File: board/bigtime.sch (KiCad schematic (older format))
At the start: 31 parts, among them IC1 NPIC6C596A, IC2 TPS62152, P1 CONN_IN, P2 CONN_OUT, U1 SA40-19, X1 MOUNTING_HOLE, X2 MOUNTING_HOLE, X3 MOUNTING_HOLE, X4 MOUNTING_HOLE

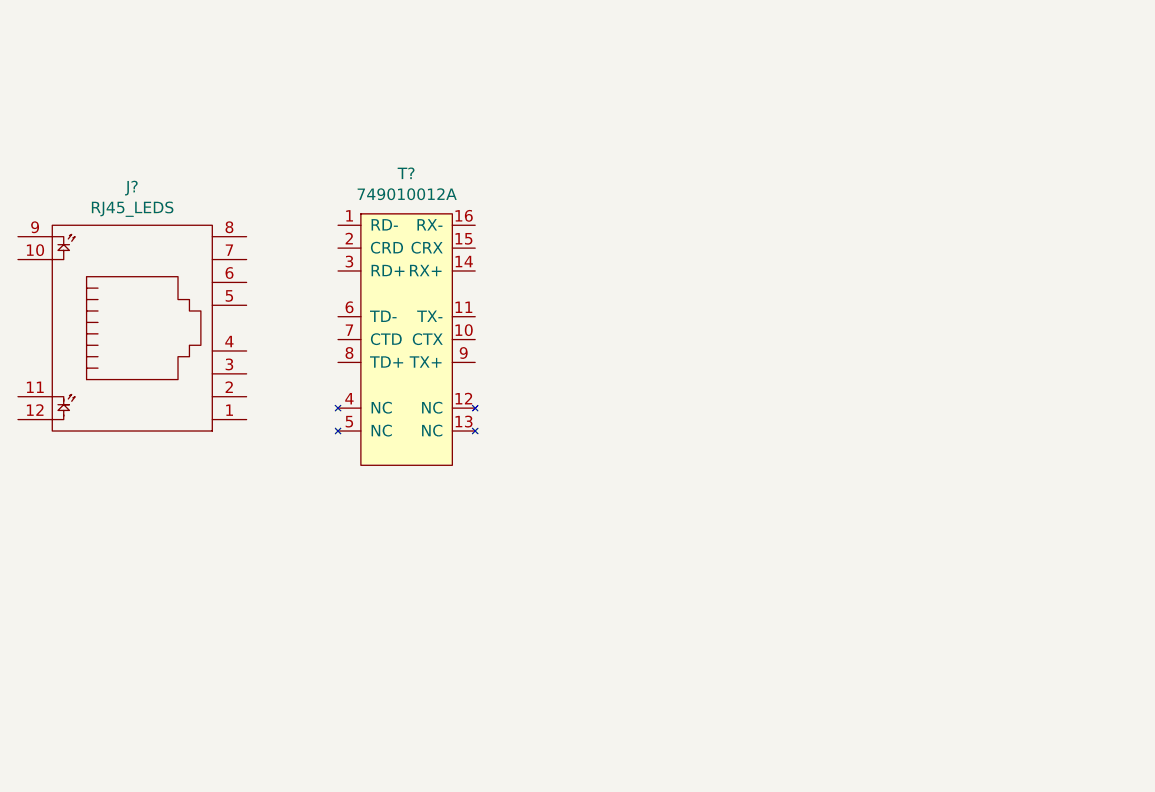
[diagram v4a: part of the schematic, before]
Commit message: separate sheet for ethernet
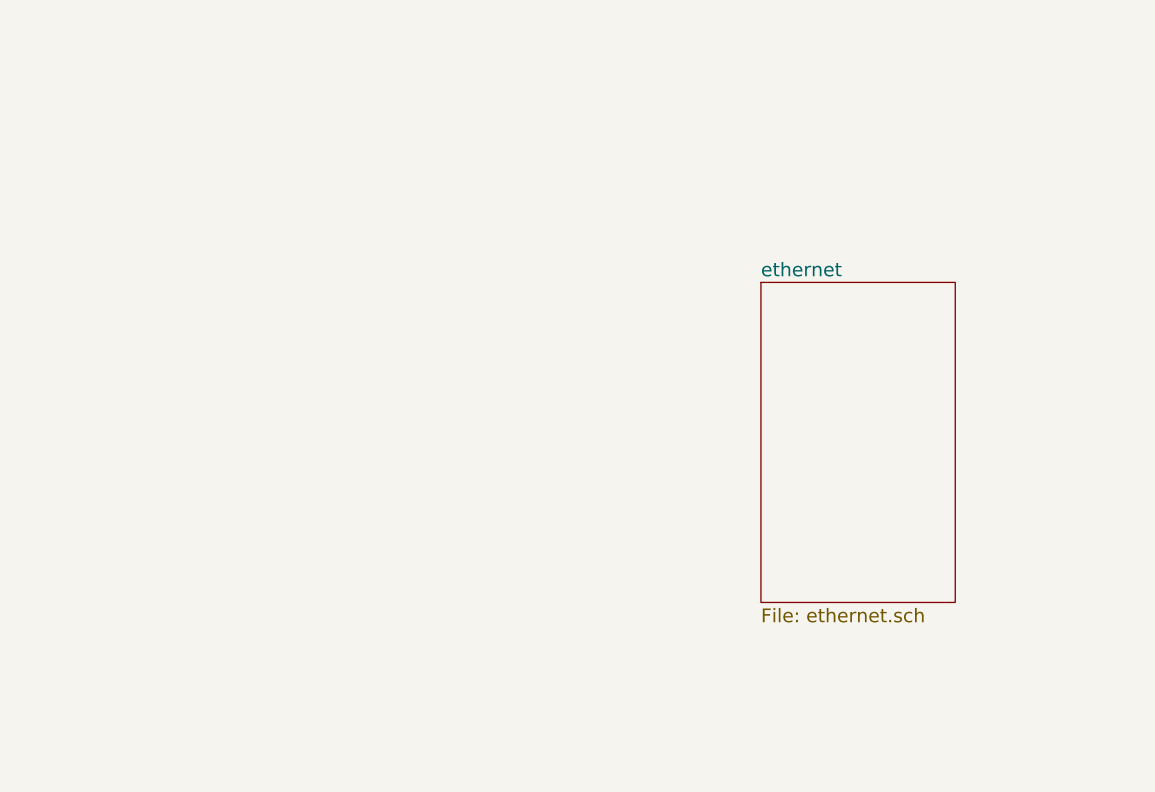
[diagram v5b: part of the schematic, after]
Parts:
- removed J?: RJ45_LEDS, symbol RJ45_LEDS
- removed T?: 749010012A, agg:749010012A, symbol 749010012A
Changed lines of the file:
@@
 $Descr A4 11693 8268
 encoding utf-8
-Sheet 1 1
+Sheet 1 2
 Title ""
 Date ""
@@
 Text Notes 8750 3500 0    60   ~ 0
 160mA nominal
-$Comp
-L RJ45_LEDS J?
-U 1 1 58B75F47
-P 1400 3600
-F 0 "J?" V 2017 3600 50  0000 C CNN
-F 1 "RJ45_LEDS" V 1926 3600 50  0000 C CNN
-F 2 "" H -1250 800 50  0001 C CNN
-F 3 "" H -1250 800 50  0001 C CNN
-	1    1400 3600
-	0    -1   -1   0
-$EndComp
-$Comp
-L 749010012A T?
-U 1 1 58B76848
-P 2600 3650
-F 0 "T?" H 2600 4375 50  0000 C CNN
-F 1 "749010012A" H 2600 4284 50  0000 C CNN
-F 2 "agg:749010012A" H -750 -300 50  0001 L CNN
-F 3 "http://katalog.we-online.de/pbs/datasheet/749010012A.pdf" H -750 -400 50  0001 L CNN
-F 4 "2422552" H -750 -500 50  0001 L CNN "Farnell"
-	1    2600 3650
-	1    0    0    -1
-$EndComp
+$Sheet
+S 4150 3400 850  1400
+U 58B736A9
+F0 "ethernet" 60
+F1 "ethernet.sch" 60
+$EndSheet
 $EndSCHEMATC

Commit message: Roughed out ethernet sheet
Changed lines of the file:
@@
 LIBS:749010012a
 LIBS:ksz8081rnx
+LIBS:max5969x
+LIBS:max17503
 LIBS:bigtime-cache
 EELAYER 26 0
@@
 160mA nominal
 $Sheet
-S 4150 3400 850  1400
+S 4150 3400 1350 1850
 U 58B736A9
 F0 "ethernet" 60
 F1 "ethernet.sch" 60
+F2 "RXD1" O L 4150 3600 60
+F3 "RXD0" O L 4150 3700 60
+F4 "CRS_DV" O L 4150 3800 60
+F5 "REF_CLK" O L 4150 3900 60
+F6 "TXEN" I L 4150 4000 60
+F7 "TXD1" I L 4150 4100 60
+F8 "TXD0" I L 4150 4200 60
+F9 "MDIO" B L 4150 4300 60
+F10 "MDC" I L 4150 4400 60
+F11 "TRAFFIC_LED" I L 4150 4500 60
 $EndSheet
 $EndSCHEMATC

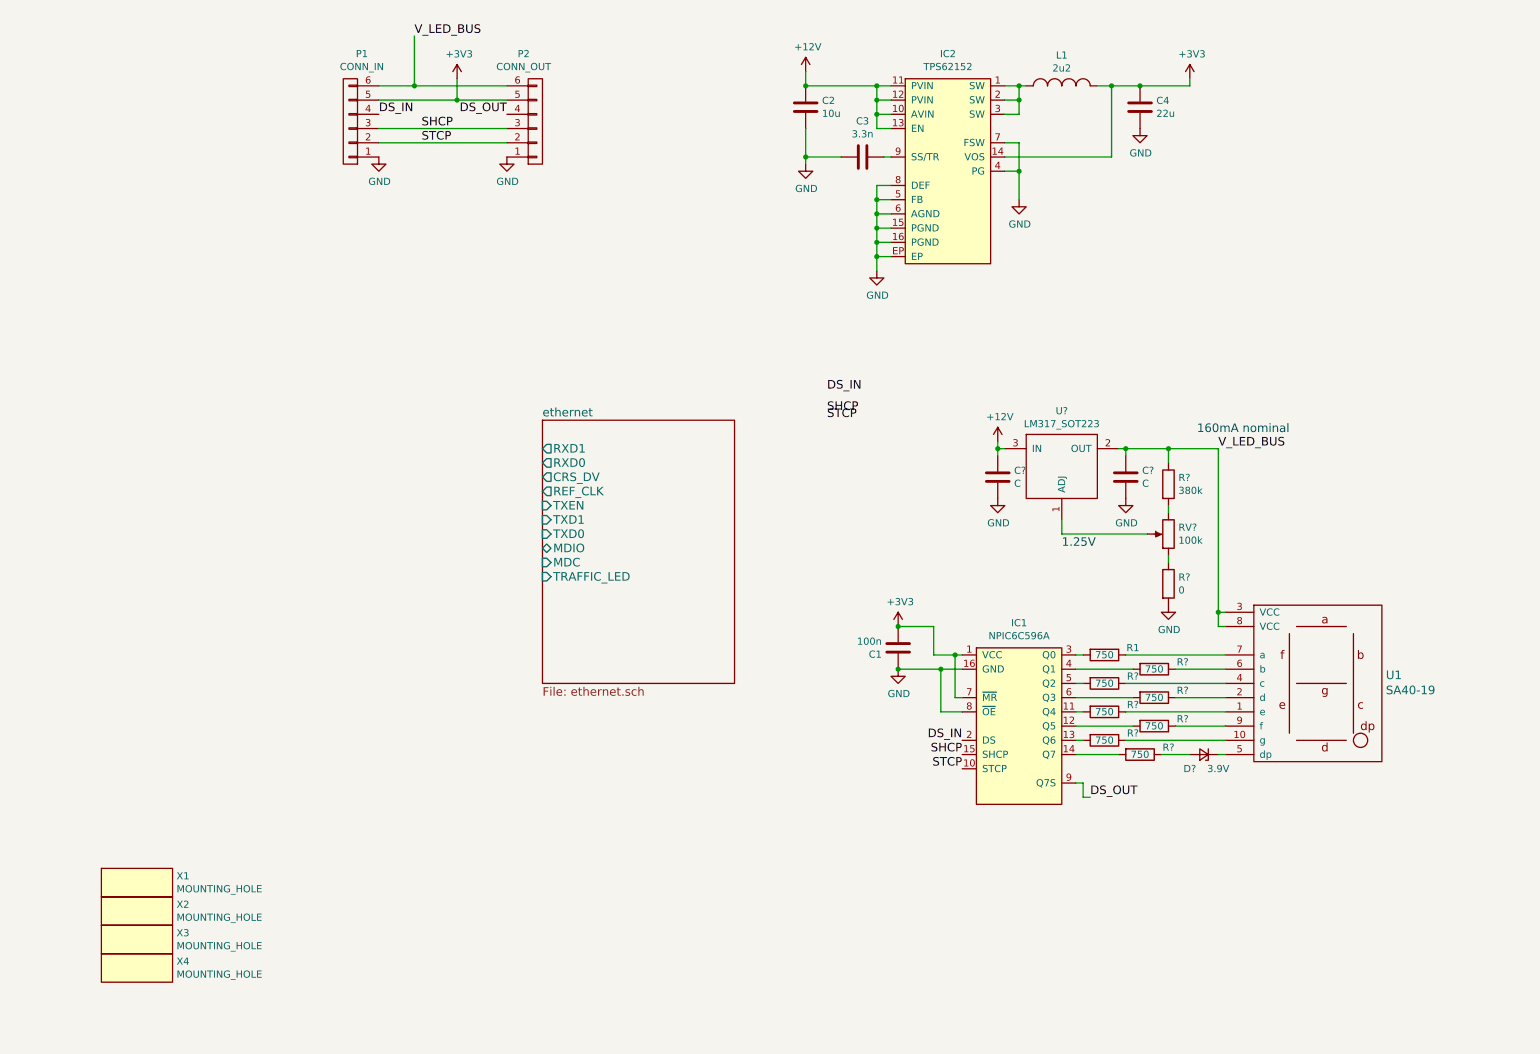
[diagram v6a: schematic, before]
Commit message: STM32 support and 25EE MAC chip
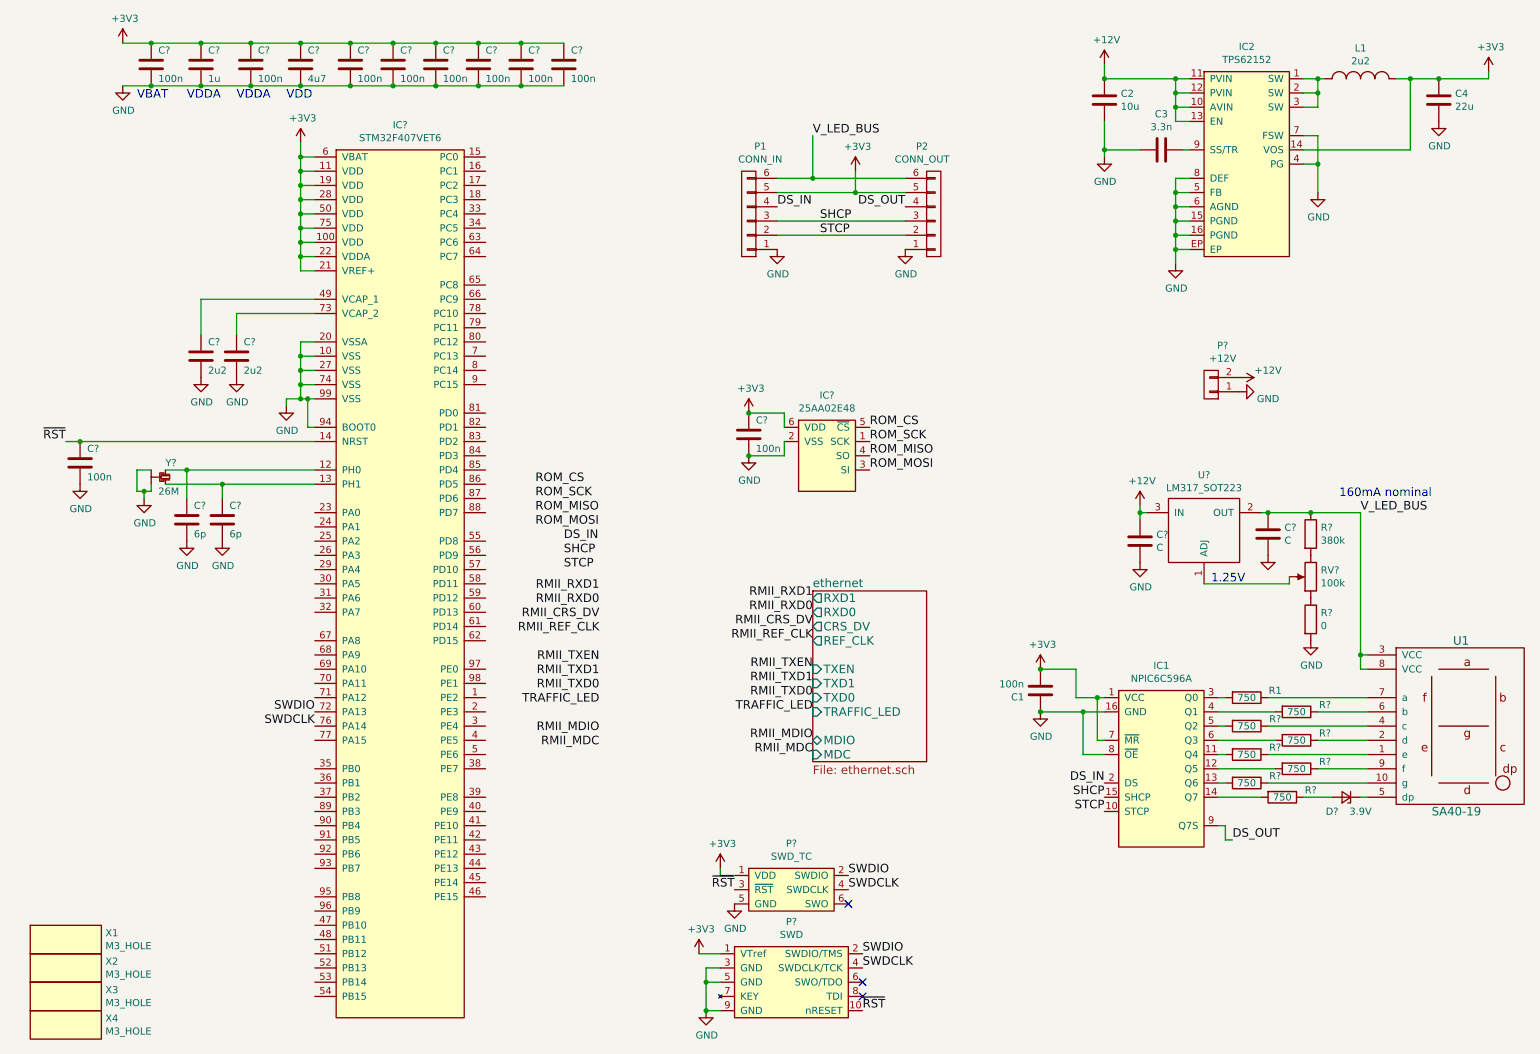
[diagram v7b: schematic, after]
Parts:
- added C? (x10): 100n, agg:0603, symbol C
- added C?: 1u, agg:0603, symbol C
- added C?: 4u7, agg:0603, symbol C
- added C? (x2): 2u2, agg:0603, symbol C
- added C? (x2): 6p, agg:0603, symbol C
- added IC?: STM32F407VET6, agg:LQFP-100, symbol STM32F4xxVxTx
- added IC?: 25AA02E48, agg:SOT-23-6, symbol 25AA02E48
- added P?: +12V, symbol CONN_01X02
- added P?: SWD, agg:FTSH-105-01-F-D-K, symbol SWD
- added P?: SWD_TC, agg:TC2030-NL, symbol SWD_TC
- added Y?: 26M, agg:XTAL-20x16, symbol SMD_XTAL
- X1, X2, X3, X4: value MOUNTING_HOLE -> M3_HOLE
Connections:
- net +12V: now also P?.2 (P2)
- net +3V3: now also C?.1, C?.1, C?.1, C?.1, C?.1, C?.1, C?.1, C?.1, C?.1, C?.1, C?.1, IC?.100 (VDD), IC?.11 (VDD), IC?.19 (VDD), IC?.21 (VREF+), IC?.22 (VDDA), IC?.28 (VDD), IC?.50 (VDD), IC?.6 (VBAT), IC?.6 (VDD), IC?.75 (VDD), P?.1 (VDD), P?.1 (VTref)
- net GND: now also C?.2, C?.2, C?.2, C?.2, C?.2, C?.2, C?.2, C?.2, C?.2, C?.2, C?.2, C?.2, C?.2, C?.2, C?.2, C?.2, IC?.10 (VSS), IC?.2 (VSS), IC?.20 (VSSA), IC?.27 (VSS), IC?.74 (VSS), IC?.94 (BOOT0), IC?.99 (VSS), P?.1 (P1), P?.3 (GND), P?.5 (GND), P?.5 (GND), P?.9 (GND), Y?.2, Y?.4
- new net: C?.1, IC?.12 (PH0), Y?.1
- new net: C?.1, IC?.13 (PH1), Y?.3
- new net: C?.1, IC?.49 (VCAP_1)
- new net: C?.1, IC?.73 (VCAP_2)
- new net ROM_CS: IC?.5 (~CS)
- new net ROM_MISO: IC?.4 (SO)
- new net ROM_MOSI: IC?.3 (SI)
- new net ROM_SCK: IC?.1 (SCK)
- new net SWDCLK: IC?.76 (PA14), P?.4 (SWDCLK), P?.4 (SWDCLK/TCK)
- new net SWDIO: IC?.72 (PA13), P?.2 (SWDIO), P?.2 (SWDIO/TMS)
- new net ~RST: C?.1, IC?.14 (NRST), P?.10 (nRESET), P?.3 (~RST)
- no-connect marks 0 -> 3
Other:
- note added: "VBAT"
- note added: "VDD"
- note added: "VDDA"
- moved on the sheet: C1, C2, C3, C4, C?, D?, IC1, IC2, L1, P1, P2, R1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

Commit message: test points, footprints, usb
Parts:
- added C44, C45: 15p, agg:0603, symbol C
- added J2: MICROUSB, agg:MICROUSB_MOLEX_47589-0001, symbol MICROUSB
- added R29: 10k, agg:0603, symbol R
- added TP1: +3.3V, agg:SIL-254P-01, symbol TEST
- added TP2: RESET, agg:SIL-254P-01, symbol TEST
- added Y3: 32.768k, footprints:XTAL_1206, symbol Crystal
- C21, C22: renamed from C?; footprint (none) -> agg:0603
- P1, P2: footprint agg:SIL-254P-06 -> Connect:IDC_Header_Straight_6pins
- P3: renamed from P?; footprint (none) -> Connect:BARREL_JACK
- R2, R3: renamed from R?; footprint (none) -> agg:0603
- gave numbers to parts that had none: 31
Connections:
- net +3V3: now also TP1.1
- net GND: now also C44.2, C45.2, J2.5 (GND)
- net ~RST: now also TP2.1
- net at IC4.8 (PC14): now also C45.1, Y3.1
- net at IC4.9 (PC15): now also C44.1, Y3.2
- new net: J2.1 (VCC), R29.2
- new net USB_D+: J2.3 (D+)
- new net USB_D-: J2.2 (D-)
- new net USB_VBUS: R29.1
- no-connect marks 3 -> 5
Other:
- moved on the sheet: C17, IC3, P1, P2, P3
